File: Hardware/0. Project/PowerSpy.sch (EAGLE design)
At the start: 68 parts, among them IC1 CP2102N-A01-GQFN28, P1 39-30-04_S, T1 SS8050, T2 SS8050, U1 ESP32-WROOM-32D, U2 HLK-PM01, U3 NCP1117ST33T3G, U4 ADS1115IDGST, X1 USB Micro B, X2 4T PJ-321, X3 4T PJ-321

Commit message: Schematic updated
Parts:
- added F1, F5: 200 mA, fuse:QPL
- added F4, F6: SF70E, fuse:LITTLEFUSE
- added LED1: IN-PI556FCH, LED RGB SMD:IN-PI556FCH
- added R32, R33, R34, R35: 130VRMS, varistor:VARISTORS05K11
- added R36: 50R (5%), rcl:R-EU_R0603
- added R37: 10k (5%), rcl:R-EU_R0402
- added S3: TL3302AF180QG, Push Button:434121050816
- R15: value 130VRMS -> 150R (5%); device varistor:VARISTORS05K11 -> rcl:R-EU_R0603
- R19: value 130VRMS -> 50R (5%); device varistor:VARISTORS05K11 -> rcl:R-EU_R0603
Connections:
- removed net PROTECTIVE_EARTH: P1-4.P
- new net BUTTON_PROG: R37.2, S3.2
- new net LED_BLUE: R36.1
- new net LED_GREEN: R19.1
- new net LED_RED: R15.1
- new net N$17: F1.1, F4.1
- new net N$21: LED1.AG1, R19.2
- new net N$23: F5.2, P1-1.P
- new net N$24: F2.2, P1-2.P
- new net N$25: F1.2, P1-3.P
- new net N$26: LED1.AB3, R36.2
- new net N$3: LED1.AR2, R15.2
- new net PE: P1-4.P, R32.2, R33.2, R34.2
- net +4.1V: now also R37.1
- net GND: now also LED1.KB4, LED1.KG6, LED1.KR5, S3.1; no longer R15.2, R19.2
- net L1_VOLTAGE: now also F6.2, R33.1, R35.1, U2.AC1; no longer F2.2, P1-1.P, R15.1
- net L2_VOLTAGE: now also F3.2, R3.1, R34.1; no longer P1-3.P, R19.1
- net N$4: now also F5.1, F6.1; no longer F3.2, R3.1, U2.AC1
- net NEUTRAL: now also F4.2, R32.1, R35.2; no longer P1-2.P
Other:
- note added: "Surge & Transient Protection"
- note added: "Thermal Protection"
- note added: "USER INTERFACE"
- moved on the sheet: C1, C12, C13, C14, C2, C5, C7, C8, C9, D5, F2, F3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

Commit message: Schematic done. PCB layout started
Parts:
- added R38: 10k (5%), rcl:R-EU_R0603
- added R39, R40: 1M (5%), rcl:R-EU_R0603
- C1: value 100nF -> 100nF/50V (10%); device rcl:C-EUC0603 -> rcl:C-EUC0603K
- C10, C13: value 100nF/50V(10%) -> 100nF/50V (10%); device rcl:C-EUC0402 -> rcl:C-EUC0603K
- C11: value 22uF/10V(20%) -> 10nF/50V (10%); device rcl:C-EUC0402 -> rcl:C-EUC0603K
- C12: value 10nF/50V(10%) -> 4.7uF/6.3V (10%); device rcl:C-EUC0402 -> rcl:C-EUC0603K
- C14: value 10nF/50V(10%) -> 100nF/50V (10%); device rcl:C-EUC0402 -> rcl:C-EUC0603K
- C15, C8: value 22uF/10V(20%) -> 100nF/50V (10%); device rcl:C-EUC0402 -> rcl:C-EUC0603K
- C2: value 10uF -> 10uF/6.3V (20%); device rcl:C-EUC0603 -> rcl:C-EUC0603K
- C3: value 4.7uF/6.3V(10%) -> 100nF/50V (10%); device rcl:C-EUC0402 -> rcl:C-EUC0603K
- C4: value 100nF/50V(10%) -> 10uF/6.3V (20%); device rcl:C-EUC0402 -> rcl:C-EUC0603K
- C5: value 10uF -> 22uF/10V (20%); device rcl:C-EUC0603 -> rcl:C-EUC0603K
- C6, C9: value 100nF/50V(10%) -> 22uF/10V (20%); device rcl:C-EUC0402 -> rcl:C-EUC0603K
- C7: value 100nF -> 10nF/50V (10%); device rcl:C-EUC0603 -> rcl:C-EUC0603K
- D1: value ESD5V0D5B -> BAT760; device ESD5V0D5B:ESD5V0D5B -> diode:DIODE-SOD323-W
- D2, D3: value ESD5V0D5B -> BAV99; device ESD5V0D5B:ESD5V0D5B -> BAV99:BAV99
- D5: value BAT760 -> ESD5V0D5B; device diode:DIODE-SOD323-W -> ESD5V0D5B:ESD5V0D5B
- D6, D7: value BAV99 -> ESD5V0D5B; device BAV99:BAV99 -> ESD5V0D5B:ESD5V0D5B
- F2: value 200 mA -> SF70E; device fuse:QPL -> fuse:LITTLEFUSE
- F3: value SF70E -> 200 mA; device fuse:LITTLEFUSE -> fuse:QPL
- P1: value 39-30-04_S -> Mini-Fit 4T
- R1: value 22.1k (5%) -> 10k (5%); device rcl:R-EU_R0402 -> rcl:R-EU_R0603
- R10, R8, R9: value 10k (5%) -> S05K130; device rcl:R-EU_R0402 -> varistor:VARISTORS05K11
- R11, R12, R13: value 10k (5%) -> 10k (1%); device rcl:R-EU_R0402 -> rcl:R-EU_R0603
- R14: value (none) -> 10k (1%)
- R15: value 150R (5%) -> 220k (1%)
- R16: value 10k (5%) -> 220k (1%); device rcl:R-EU_R0402 -> rcl:R-EU_R0603
- R17: value 10k (5%) -> 100k (1%); device rcl:R-EU_R0402 -> rcl:R-EU_R0603
- R18, R25, R26: value (none) -> 100k (1%)
- R19: value 50R (5%) -> 47R (5%)
- R2: value 47.5k (5%) -> S05K230; device rcl:R-EU_R0402 -> varistor:VARISTORS05K11
- R20, R28: value (none) -> 1k (1%)
- R21, R22: value (none) -> 10k (5%)
- R23: value (none) -> 220k (1%)
- R24: value 47R (5%) -> 220k (1%); device rcl:R-EU_R0402 -> rcl:R-EU_R0603
- R27: value (none) -> 47R (5%)
- R29: value 47R (5%) -> 2k (5%); device rcl:R-EU_R0402 -> rcl:R-EU_R0603
- R3: value 130VRMS -> S05K130
- R30, R31: device rcl:R-EU_R0402 -> rcl:R-EU_R0603
- R32: value 130VRMS -> 10k (5%)(NC); device varistor:VARISTORS05K11 -> rcl:R-EU_R0603
- R33: value 130VRMS -> 22.1k (5%); device varistor:VARISTORS05K11 -> rcl:R-EU_R0603
- R34: value 130VRMS -> 10k (5%); device varistor:VARISTORS05K11 -> rcl:R-EU_R0603
- R35: value 130VRMS -> 0R (5%); device varistor:VARISTORS05K11 -> rcl:R-EU_R0603
- R36: value 50R (5%) -> 0R (5%)
- R37: value 10k (5%) -> 47.5k (5%); device rcl:R-EU_R0402 -> rcl:R-EU_R0603
- R4: value 2k (5%) -> 150R (5%); device rcl:R-EU_R0402 -> rcl:R-EU_R0603
- R5: value 10k (5%)(NC) -> 50R (5%); device rcl:R-EU_R0402 -> rcl:R-EU_R0603
- R6: value 0R (5%) -> 50R (5%); device rcl:R-EU_R0402 -> rcl:R-EU_R0603
- R7: value 0R (5%) -> S05K130; device rcl:R-EU_R0402 -> varistor:VARISTORS05K11
- U1: value ESP32-WROOM-32D -> NCP1117ST33T3G; device ESP32-WROOM-32D:ESP32-WROOM-32D -> REG1117:REG1117
- U3: value NCP1117ST33T3G -> ADS1115IDGST; device REG1117:REG1117 -> ADS1115IDGST:ADS1115IDGST
- U4: value ADS1115IDGST -> ESP32-WROOM-32D; device ADS1115IDGST:ADS1115IDGST -> ESP32-WROOM-32D:ESP32-WROOM-32D
- X1: value USB Micro B -> 4T PJ-321; device Micro USB Connector:ZX62D-B-5PA8 -> con-lumberg:1503_07
- X3: value 4T PJ-321 -> USB Micro B; device con-lumberg:1503_07 -> Micro USB Connector:ZX62D-B-5PA8
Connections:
- removed net N$13: R20.1, R21.2
- removed net N$14: R18.1, R20.2
- removed net N$15: R21.1, R22.2
- removed net N$17 (its old number): F1.1, F4.1
- new net N$27: R24.2, R25.1
- new net N$28: R25.2, R26.1
- new net N$29: R23.2, R24.1
- new net N$4: F1.1, F2.1
- net +4.1V: now also C10.1, C12.1, D2.C2, D3.C2, R1.1, R21.1, R22.1, R29.2, R31.1, U3.VDD, U4.3V3; no longer C3.1, C4.1, D6.C2, D7.C2, R10.1, R16.1, R17.1, R37.1, R4.2, U1.3V3, U4.VDD
- net 3.3V: now also C3.1, C4.1, U1.VOUT; no longer C1.1, C2.1, U3.VOUT
- net 5V: now also C1.1, C2.1, D1.C, U1.VIN; no longer C5.1, C7.1, D5.C, U3.VIN
- net ADC_ALERT: now also U3.ALERT/RDY; no longer U4.ALERT/RDY
- net ADC_CURRENT_L1: now also R39.1, U3.AIN0, U4.IO32, X1.1; no longer U4.AIN0, X2.1
- net ADC_CURRENT_L2: now also R40.1, U3.AIN2, U4.IO33, X2.1; no longer U4.AIN2, X3.1
- net ADC_SCL: now also R21.2, U3.SCL; no longer R16.2, U4.SCL
- net ADC_SDA: now also R22.2, U3.SDA; no longer R17.2, U4.SDA
- net ADC_VOLTAGE_L1: now also C7.1, R19.1, U3.AIN1, U4.IO34; no longer C12.1, R29.1, U4.AIN1
- net ADC_VOLTAGE_L2: now also C11.1, R27.1, U3.AIN3, U4.IO35; no longer C14.1, R24.1, U4.AIN3
- net BUTTON_PROG: now also R1.2, S1.2; no longer R37.2, S3.2
- net DTR: now also R34.2, T2.E; no longer R8.2, T1.E
- net EN: now also C15.1, R31.2, S3.2, T1.C, U4.EN; no longer C6.1, R10.2, S1.2, T2.C, U1.EN
- net GND: now also D2.A1, D3.A1, D5.1, D6.1, D7.1, R14.2, R32.1, R37.1, R39.2, R40.2, U3.ADDR, X3G$1.5; no longer D1.1, D2.1, D3.1, D6.A1, D7.A1, R2.1, R23.2, R28.2, R31.2, R5.1, U4.ADDR, X1G$1.5
- net IO0: now also C14.1, R30.2, T2.C; no longer C10.1, R11.2, T1.C
- net L1_VOLTAGE: now also F2.2, R10.1, R15.1, R2.1, R3.1; no longer F6.2, R27.1, R33.1, R35.1
- net L2_VOLTAGE: now also F4.2, R2.2, R23.1, R7.1, R9.1; no longer F3.2, R22.1, R3.1, R34.1
- net LED_BLUE: now also R6.1; no longer R36.1
- net LED_GREEN: now also R5.1; no longer R19.1
- net LED_RED: now also R4.1; no longer R15.1
- net N$1: now also R32.2; no longer R5.2
- net N$10: now also R36.2; no longer R7.2
- net N$11: now also C5.1, R11.2, X1.2; no longer C11.1, R12.2, X2.2
- net N$12: now also R16.2, R17.1; no longer R25.1, R26.2
- net N$16: now also D3.COM, R26.2, R27.2, R28.1; no longer D7.COM, R18.2, R23.1, R24.2
- net N$18: now also R17.2, R18.1; no longer R14.1, R25.2
- net N$19: now also R15.2, R16.1; no longer R26.1, R27.2
- net N$2: now also R29.1; no longer R4.1
- net N$20: now also D2.COM, R18.2, R19.2, R20.1; no longer D6.COM, R14.2, R28.1, R29.2
- net N$21: now also R5.2; no longer R19.2
- net N$22: now also C6.1, R12.2, R14.1, X2.2; no longer C15.1, R30.2, R31.1, X3.2
- net N$23: now also F1.2; no longer F5.2
- net N$24: now also F3.2; no longer F2.2
- net N$25: now also F5.2; no longer F1.2
- net N$26: now also R6.2; no longer R36.2
- net N$3: now also R4.2; no longer R15.2
- net N$5: now also R38.1, T2.B; no longer R9.1, T1.B
- net N$6: now also D1.A; no longer D5.A
- net N$7: now also R34.1, T1.B; no longer R8.1, T2.B
- net N$8: now also R35.2; no longer R6.2
- net N$9: now also F4.1; no longer F2.1
- net NEUTRAL: now also F6.2, R20.2, R28.2, R7.2, R8.1; no longer F4.2, R32.1, R35.2
- net PE: now also R10.2, R8.2, R9.2; no longer R32.2, R33.2, R34.2
- net RTS: now also R38.2, T1.E; no longer R9.2, T2.E
- net USB_CONNECTED: now also R33.1, R37.2; no longer R1.1, R2.2
- net USB_D+: now also D5.2, X3G$1.3; no longer D1.2, X1G$1.3
- net USB_D-: now also D6.2, X3G$1.2; no longer D2.2, X1G$1.2
- net USB_RX: now also R36.1, U4.TXD0; no longer R7.1, U1.TXD0
- net USB_TX: now also R35.1, U4.RXD0; no longer R6.1, U1.RXD0
- net VUSB: now also D7.2, R33.2, X3G$1.1; no longer D3.2, R1.2, X1G$1.1
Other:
- moved on the sheet: C1, C10, C11, C12, C13, C14, C15, C2, C3, C4, C5, C6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

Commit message: Schematic done. PCB layout almost done.
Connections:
- removed net +4.1V: C10.1, C12.1, C13.1, C8.1, C9.1, D2.C2, D3.C2, IC1.REGIN, IC1.VDD, R1.1, R11.1, R12.1, R21.1, R22.1, R29.2, R30.1, R31.1, U3.VDD, U4.3V3
- net 3.3V: now also C10.1, C12.1, C13.1, C8.1, C9.1, D2.C2, D3.C2, IC1.REGIN, IC1.VDD, R1.1, R11.1, R12.1, R21.1, R22.1, R29.2, R30.1, R31.1, U3.VDD, U4.3V3
- net ADC_ALERT: now also U4.IO19
- net ADC_SCL: now also U4.IO22
- net ADC_SDA: now also U4.IO21
- net BUTTON_PROG: now also U4.IO23
- net IO0: now also U4.IO0
- net LED_BLUE: now also U4.IO27
- net LED_GREEN: now also U4.IO26
- net LED_RED: now also U4.IO25

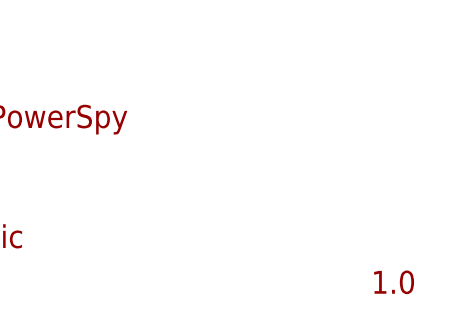
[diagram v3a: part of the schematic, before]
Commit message: 2.0 PCB created
- Board dimensions resize to match with PB075 Patola case.
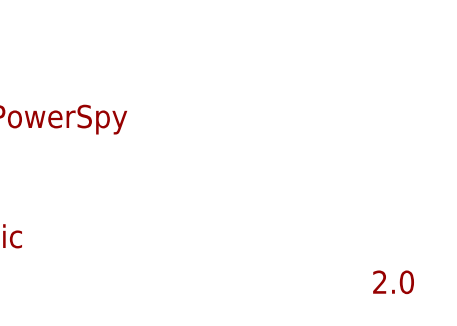
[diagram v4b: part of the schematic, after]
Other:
- note added: "2.0"
- note removed: "1.0"
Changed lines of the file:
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@@
 <?xml version="1.0" encoding="utf-8"?>
 <!DOCTYPE eagle SYSTEM "eagle.dtd">
-<eagle version="9.4.2">
+<eagle version="9.5.2">
 <drawing>
 <settings>
@@
 <setting verticaltext="up"/>
 </settings>
-<grid distance="0.025" unitdist="inch" unit="inch" style="lines" multiple="1" display="no" altdistance="0.01" altunitdist="inch" altunit="inch"/>
+<grid distance="0.1" unitdist="inch" unit="inch" style="lines" multiple="1" display="no" altdistance="0.01" altunitdist="inch" altunit="inch"/>
 <layers>
 <layer number="1" name="Top" color="4" fill="1" visible="no" active="no"/>
@@
 <text x="307.975" y="26.035" size="3.81" layer="94">Tiago Silva</text>
 <text x="290.83" y="19.685" size="2.54" layer="94">github.com/TiagoPaulaSilva/PowerSpy</text>
-<text x="377.825" y="1.27" size="2.54" layer="94" ratio="5">1.0</text>
+<text x="377.825" y="1.27" size="2.54" layer="94" ratio="5">2.0</text>
 <text x="306.705" y="6.35" size="2.54" layer="94" ratio="5">Complete Schematic</text>
 <text x="272.415" y="166.37" size="1.778" layer="97">AC/DC Converter Module</text>

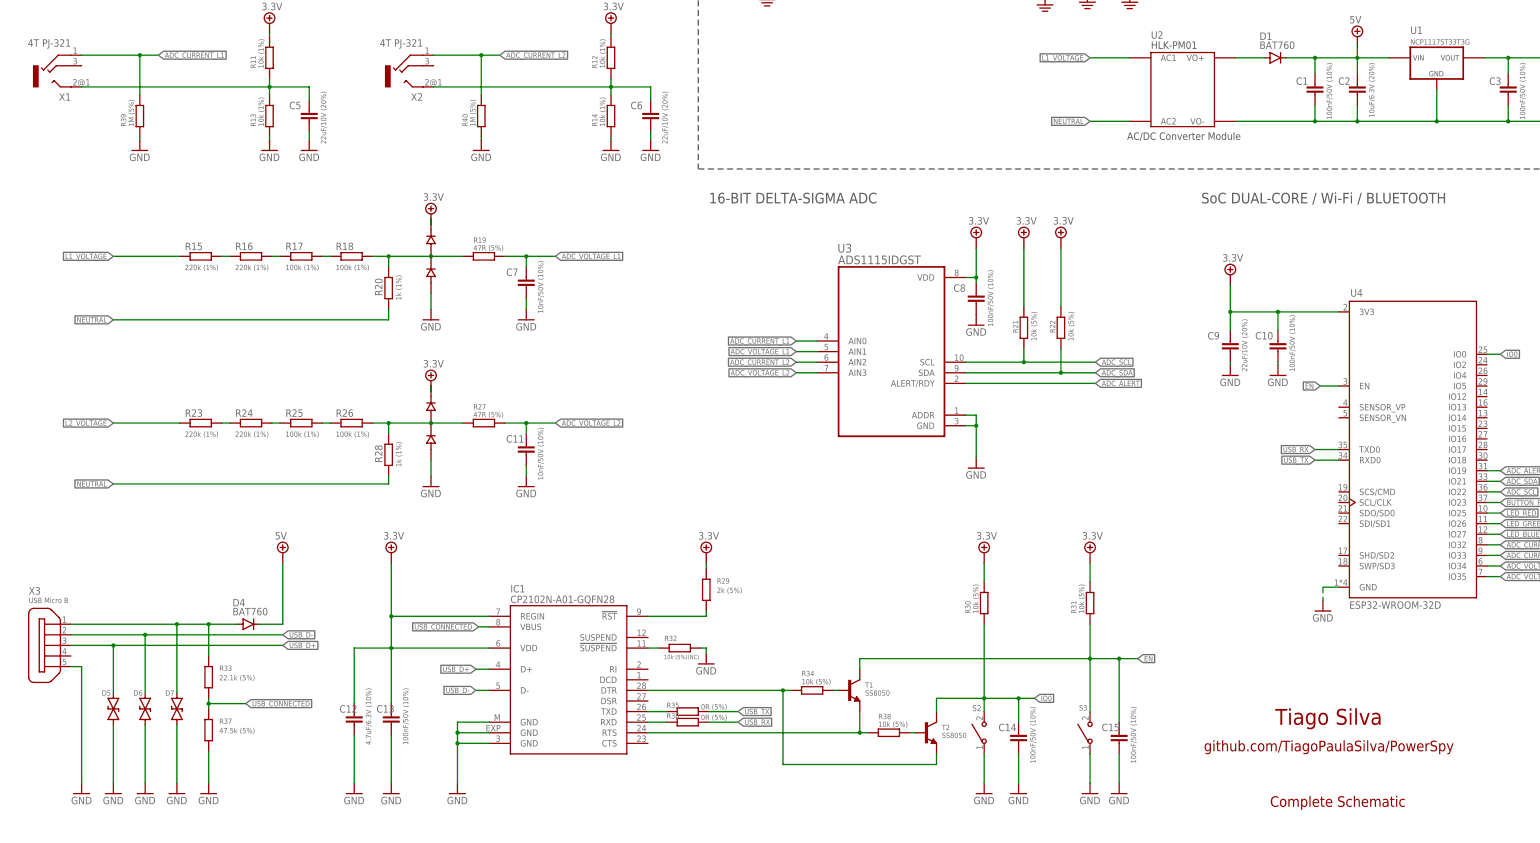
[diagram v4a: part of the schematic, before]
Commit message: VCC/2 set point added to voltage phase measure channel (WIP)
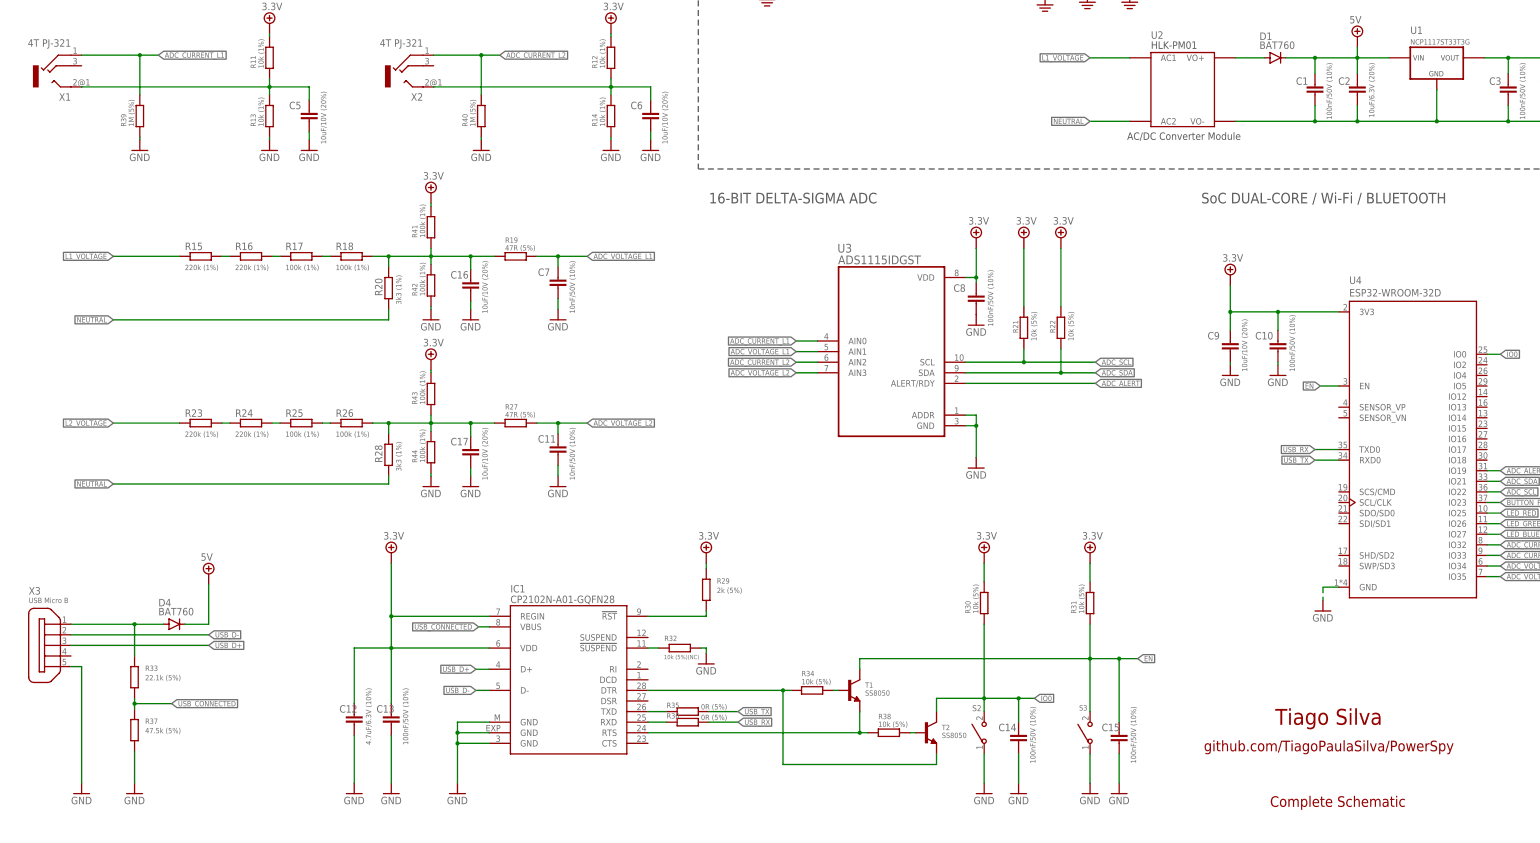
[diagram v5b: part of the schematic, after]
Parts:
- removed D2, D3: BAV99, BAV99:BAV99
- removed D5, D6, D7: ESD5V0D5B, ESD5V0D5B:ESD5V0D5B
- added C16, C17: 10uF/10V (20%), rcl:C-EUC0603K
- added R41, R42, R43, R44: 100k (1%), rcl:R-EU_R0603
- C5, C6, C9: value 22uF/10V (20%) -> 10uF/10V (20%)
- R20, R28: value 1k (1%) -> 3k3 (1%)
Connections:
- net 3.3V: now also R41.1, R43.1; no longer D2.C2, D3.C2
- net GND: now also C16.2, C17.2, R42.2, R44.2; no longer D2.A1, D3.A1, D5.1, D6.1, D7.1
- net N$16: now also C17.1, R43.2, R44.1; no longer D3.COM
- net N$20: now also C16.1, R41.2, R42.1; no longer D2.COM
- net USB_D+: no longer D5.2
- net USB_D-: no longer D6.2
- net VUSB: no longer D7.2
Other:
- moved on the sheet: C11, C7, D4, R19, R27, R33, R37

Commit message: New analog front-end design for voltage measurement
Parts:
- removed C16, C17: 10uF/10V (20%), rcl:C-EUC0603K
- added C18, C20: 10uF/10V (20%), rcl:C-EUC0603K
- added C19: 100nF/50V (10%), rcl:C-EUC0603K
- added IC3: LM324D, linear:LM324D
- added R45, R46, R49, R50: 100k (1%), rcl:R-EU_R0603
- added R47: 220R (5%), rcl:R-EU_R0603
- R41, R44: value 100k (1%) -> 220R (5%)
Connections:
- new net +4.1V: C20.1, IC3P.V+
- new net N$13: IC3A.-IN, IC3A.OUT, R47.2
- new net N$14: C18.1, C19.1, IC3A.+IN, R45.2, R46.1
- new net N$15: IC3B.OUT, R19.2, R49.1
- new net N$30: IC3B.-IN, R49.2, R50.1
- new net N$31: R18.2, R20.1, R41.2
- new net N$32: IC3B.+IN, R41.1
- new net N$33: IC3C.-IN, R42.2, R43.1
- new net N$34: IC3C.+IN, R44.1
- net 3.3V: now also R45.1; no longer R41.1, R43.1
- net GND: now also C18.2, C19.2, C20.2, IC3P.V-, R46.2; no longer C16.2, C17.2, R42.2, R44.2
- net N$16: now also R44.2; no longer C17.1, R27.2, R43.2, R44.1
- net N$20: now also IC3C.OUT, R27.2; no longer C16.1, R18.2, R19.2, R20.1, R41.2
- net NEUTRAL: no longer R20.2, R28.2
- net PE: now also R20.2, R28.2, R43.2, R47.1, R50.2
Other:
- note added: "VIRTUAL GROUND REFERENCE"
- moved on the sheet: C1, C10, C11, C12, C13, C14, C15, C2, C3, C4, C5, C6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
